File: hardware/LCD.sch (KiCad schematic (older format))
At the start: 23 parts, among them IC1 TPS61169DCKR, IC2 TPD4E001DRLR, IC3 AR1021-I/SS, U3 DS90CF364AMTD

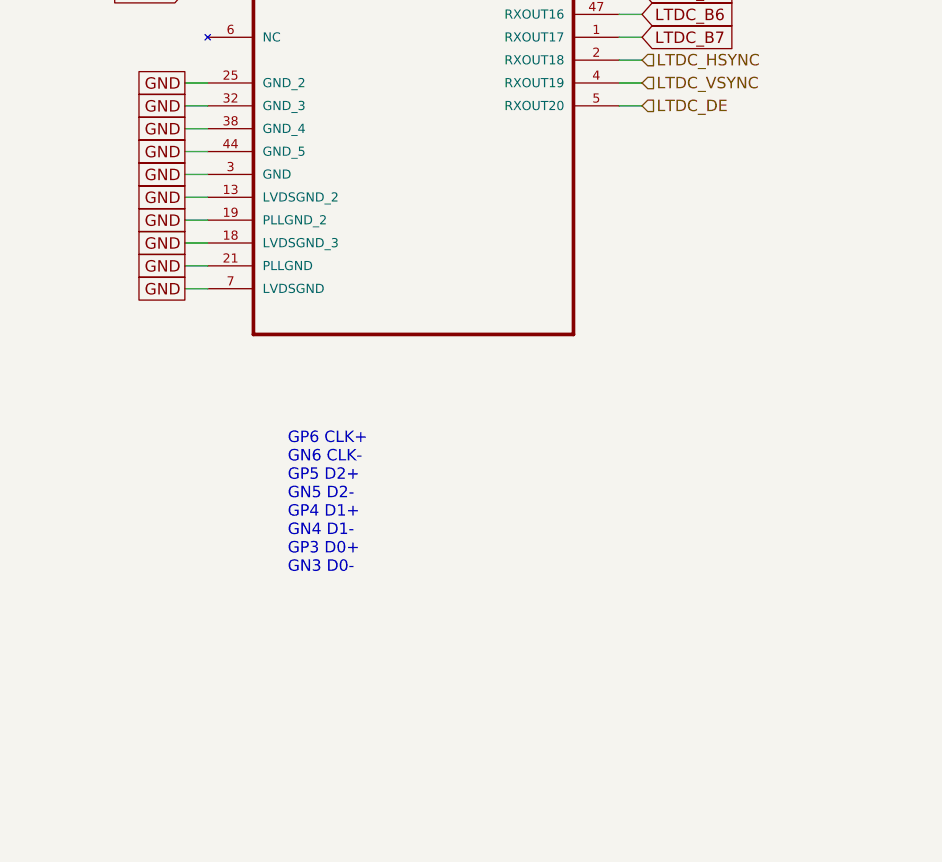
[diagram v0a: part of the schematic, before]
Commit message: Adding decoupling capacitors, termination resoistors for LVDS IN
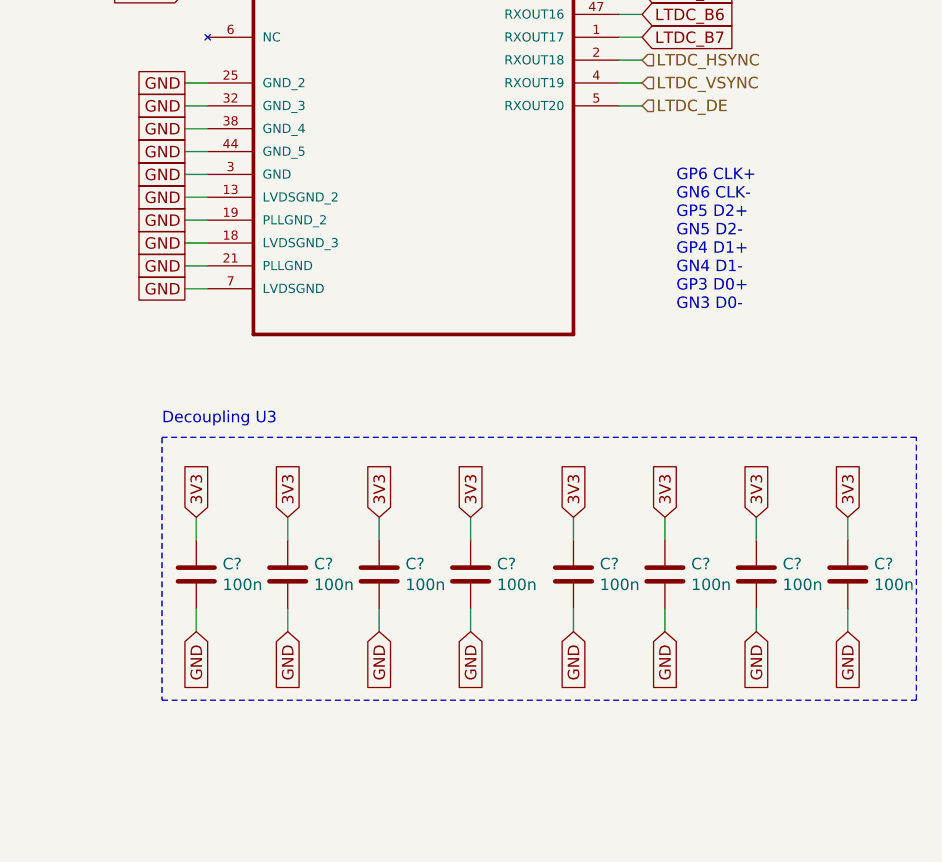
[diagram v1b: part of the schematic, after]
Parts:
- added C? (x8): 100n, symbol antena:C
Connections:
- net 3V3: now also C?.1, C?.1, C?.1, C?.1, C?.1, C?.1, C?.1, C?.1
- net GND: now also C?.2, C?.2, C?.2, C?.2, C?.2, C?.2, C?.2, C?.2
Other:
- note added: "Decoupling U3"
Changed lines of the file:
@@
 Wire Wire Line
 	9900 2350 10000 2350
-Text Notes 8450 5900 0    50   ~ 0
+Text Notes 10150 4750 0    50   ~ 0
 GP6 CLK+\nGN6 CLK-\nGP5 D2+\nGN5 D2-\nGP4 D1+\nGN4 D1-\nGP3 D0+\nGN3 D0-
 Text GLabel 8000 2350 0    50   Output ~ 0
@@
 Wire Wire Line
 	5500 7550 5650 7550
+Text GLabel 8000 3350 0    50   Input ~ 0
+~RESET
+Text GLabel 9700 5650 1    50   Input ~ 0
+3V3
+Text GLabel 9700 6150 3    50   Input ~ 0
+GND
+$Comp
+L antena:C C?
+U 1 1 5E384C70
+P 9700 5900
+AR Path="/5E22D431/5E384C70" Ref="C?"  Part="1"
+AR Path="/5E224865/5E384C70" Ref="C?"  Part="1"
+F 0 "C?" H 9815 5946 50  0000 L CNN
+F 1 "100n" H 9815 5855 50  0000 L CNN
+F 2 "" H 9738 5750 50  0001 C CNN
+F 3 "~" H 9700 5900 50  0001 C CNN
+	1    9700 5900
+	1    0    0    -1
+$EndComp
+Wire Wire Line
+	9700 5650 9700 5750
+Wire Wire Line
+	9700 6050 9700 6150
+Text GLabel 10100 5650 1    50   Input ~ 0
+3V3
+Text GLabel 10100 6150 3    50   Input ~ 0
+GND
+$Comp
+L antena:C C?
+U 1 1 5E384C7B
+P 10100 5900
+AR Path="/5E22D431/5E384C7B" Ref="C?"  Part="1"
+AR Path="/5E224865/5E384C7B" Ref="C?"  Part="1"
+F 0 "C?" H 10215 5946 50  0000 L CNN
+F 1 "100n" H 10215 5855 50  0000 L CNN
+F 2 "" H 10138 5750 50  0001 C CNN
+F 3 "~" H 10100 5900 50  0001 C CNN
+	1    10100 5900
+	1    0    0    -1
+$EndComp
+Wire Wire Line
+	10100 5650 10100 5750
+Wire Wire Line
+	10100 6050 10100 6150
+Text GLabel 10500 5650 1    50   Input ~ 0
+3V3
+Text GLabel 10500 6150 3    50   Input ~ 0
+GND
+$Comp
+L antena:C C?
+U 1 1 5E384C86
+P 10500 5900
+AR Path="/5E22D431/5E384C86" Ref="C?"  Part="1"
+AR Path="/5E224865/5E384C86" Ref="C?"  Part="1"
+F 0 "C?" H 10615 5946 50  0000 L CNN
+F 1 "100n" H 10615 5855 50  0000 L CNN
+F 2 "" H 10538 5750 50  0001 C CNN
+F 3 "~" H 10500 5900 50  0001 C CNN
+	1    10500 5900
+	1    0    0    -1
+$EndComp
+Wire Wire Line
+	10500 5650 10500 5750
+Wire Wire Line
+	10500 6050 10500 6150
+Text GLabel 10900 5650 1    50   Input ~ 0
+3V3
+Text GLabel 10900 6150 3    50   Input ~ 0
+GND
+$Comp
+L antena:C C?
+U 1 1 5E384C91
+P 10900 5900
+AR Path="/5E22D431/5E384C91" Ref="C?"  Part="1"
+AR Path="/5E224865/5E384C91" Ref="C?"  Part="1"
+F 0 "C?" H 11015 5946 50  0000 L CNN
+F 1 "100n" H 11015 5855 50  0000 L CNN
+F 2 "" H 10938 5750 50  0001 C CNN
+F 3 "~" H 10900 5900 50  0001 C CNN
+	1    10900 5900
+	1    0    0    -1
+$EndComp
+Wire Wire Line
+	10900 5650 10900 5750
+Wire Wire Line
+	10900 6050 10900 6150
+Text GLabel 8050 5650 1    50   Input ~ 0
+3V3
+Text GLabel 8050 6150 3    50   Input ~ 0
+GND
+$Comp
+L antena:C C?
+U 1 1 5E384C9C
+P 8050 5900
+AR Path="/5E22D431/5E384C9C" Ref="C?"  Part="1"
+AR Path="/5E224865/5E384C9C" Ref="C?"  Part="1"
+F 0 "C?" H 8165 5946 50  0000 L CNN
+F 1 "100n" H 8165 5855 50  0000 L CNN
+F 2 "" H 8088 5750 50  0001 C CNN
+F 3 "~" H 8050 5900 50  0001 C CNN
+	1    8050 5900
+	1    0    0    -1
+$EndComp
+Wire Wire Line
+	8050 5650 8050 5750
+Wire Wire Line
+	8050 6050 8050 6150
+Text GLabel 8450 5650 1    50   Input ~ 0
+3V3
+Text GLabel 8450 6150 3    50   Input ~ 0
+GND
+$Comp
+L antena:C C?
+U 1 1 5E384CA7
+P 8450 5900
+AR Path="/5E22D431/5E384CA7" Ref="C?"  Part="1"
+AR Path="/5E224865/5E384CA7" Ref="C?"  Part="1"
+F 0 "C?" H 8565 5946 50  0000 L CNN
+F 1 "100n" H 8565 5855 50  0000 L CNN
+F 2 "" H 8488 5750 50  0001 C CNN
+F 3 "~" H 8450 5900 50  0001 C CNN
+	1    8450 5900
+	1    0    0    -1
+$EndComp
+Wire Wire Line
+	8450 5650 8450 5750
+Wire Wire Line
+	8450 6050 8450 6150
+Text GLabel 8850 5650 1    50   Input ~ 0
+3V3
+Text GLabel 8850 6150 3    50   Input ~ 0
+GND
+$Comp
+L antena:C C?
+U 1 1 5E384CB2
+P 8850 5900
+AR Path="/5E22D431/5E384CB2" Ref="C?"  Part="1"
+AR Path="/5E224865/5E384CB2" Ref="C?"  Part="1"
+F 0 "C?" H 8965 5946 50  0000 L CNN
+F 1 "100n" H 8965 5855 50  0000 L CNN
+F 2 "" H 8888 5750 50  0001 C CNN
+F 3 "~" H 8850 5900 50  0001 C CNN
+	1    8850 5900
+	1    0    0    -1
+$EndComp
+Wire Wire Line
+	8850 5650 8850 5750
+Wire Wire Line
+	8850 6050 8850 6150
+Text GLabel 9250 5650 1    50   Input ~ 0
+3V3
+Text GLabel 9250 6150 3    50   Input ~ 0
+GND
+$Comp
+L antena:C C?
+U 1 1 5E384CBD
+P 9250 5900
+AR Path="/5E22D431/5E384CBD" Ref="C?"  Part="1"
+AR Path="/5E224865/5E384CBD" Ref="C?"  Part="1"
+F 0 "C?" H 9365 5946 50  0000 L CNN
+F 1 "100n" H 9365 5855 50  0000 L CNN
+F 2 "" H 9288 5750 50  0001 C CNN
+F 3 "~" H 9250 5900 50  0001 C CNN
+	1    9250 5900
+	1    0    0    -1
+$EndComp
+Wire Wire Line
+	9250 5650 9250 5750
+Wire Wire Line
+	9250 6050 9250 6150
+Wire Notes Line
+	11200 6450 11200 5300
+Wire Notes Line
+	11200 5300 7900 5300
+Wire Notes Line
+	7900 5300 7900 6450
+Wire Notes Line
+	7900 6450 11200 6450
 Wire Bus Line
 	6175 2700 6175 3200
@@
 Wire Bus Line
 	6175 1900 6175 2400
-Text GLabel 8000 3350 0    50   Input ~ 0
-~RESET
+Text Notes 7900 5250 0    50   ~ 0
+Decoupling U3
 $EndSCHEMATC

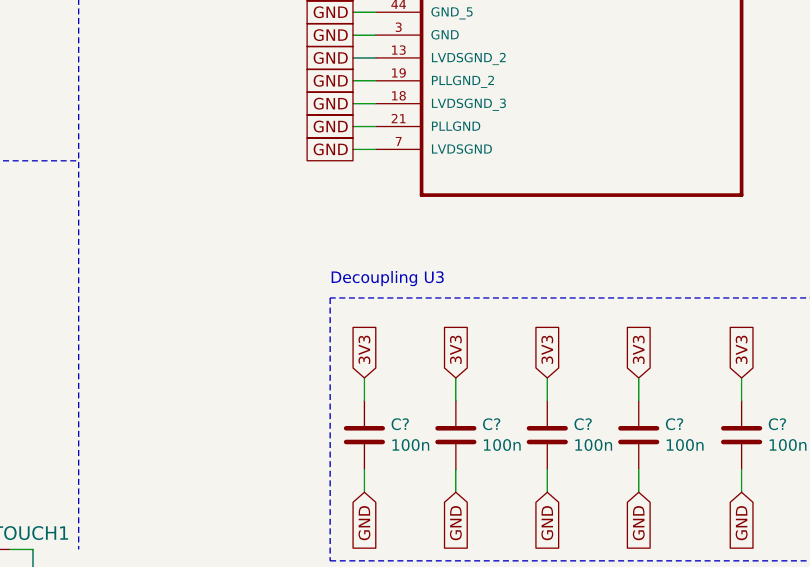
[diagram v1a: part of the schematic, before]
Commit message: Adding selection resistors
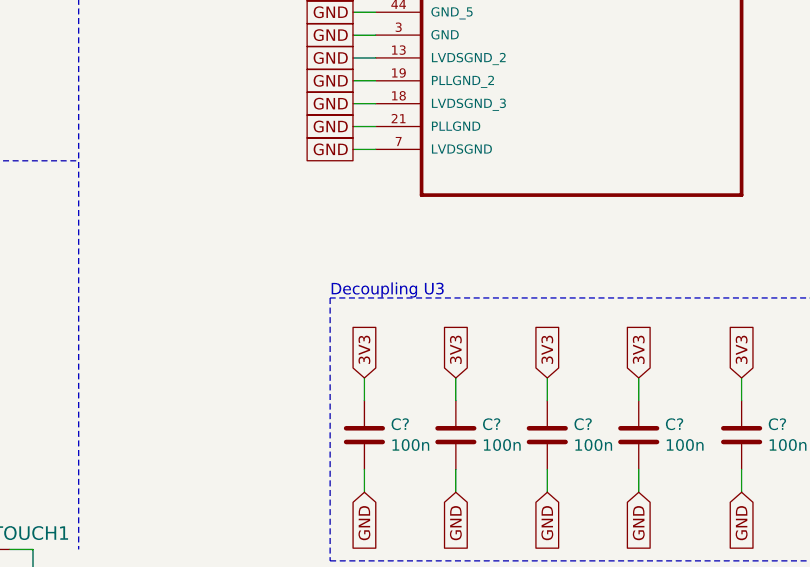
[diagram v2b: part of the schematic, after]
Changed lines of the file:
@@
 Wire Notes Line
 	7900 6450 11200 6450
+Text Notes 7900 5300 0    50   ~ 0
+Decoupling U3
 Wire Bus Line
 	6175 2700 6175 3200
@@
 Wire Bus Line
 	6175 1900 6175 2400
-Text Notes 7900 5250 0    50   ~ 0
-Decoupling U3
 $EndSCHEMATC

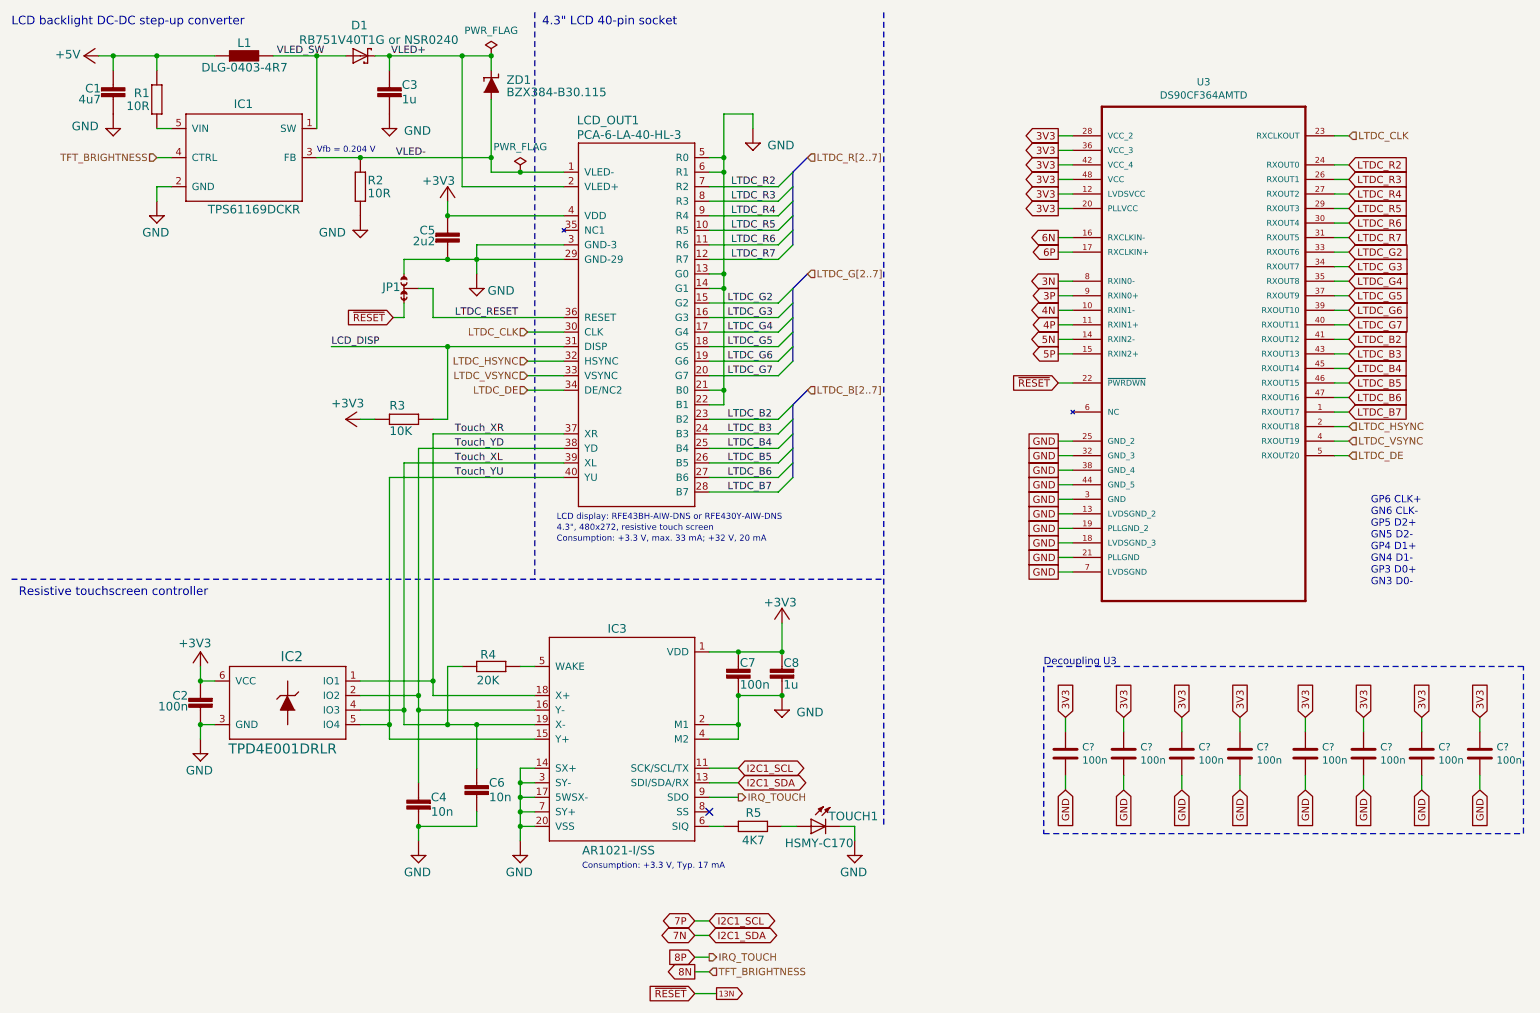
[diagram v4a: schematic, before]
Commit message: Adding ULX3S connections
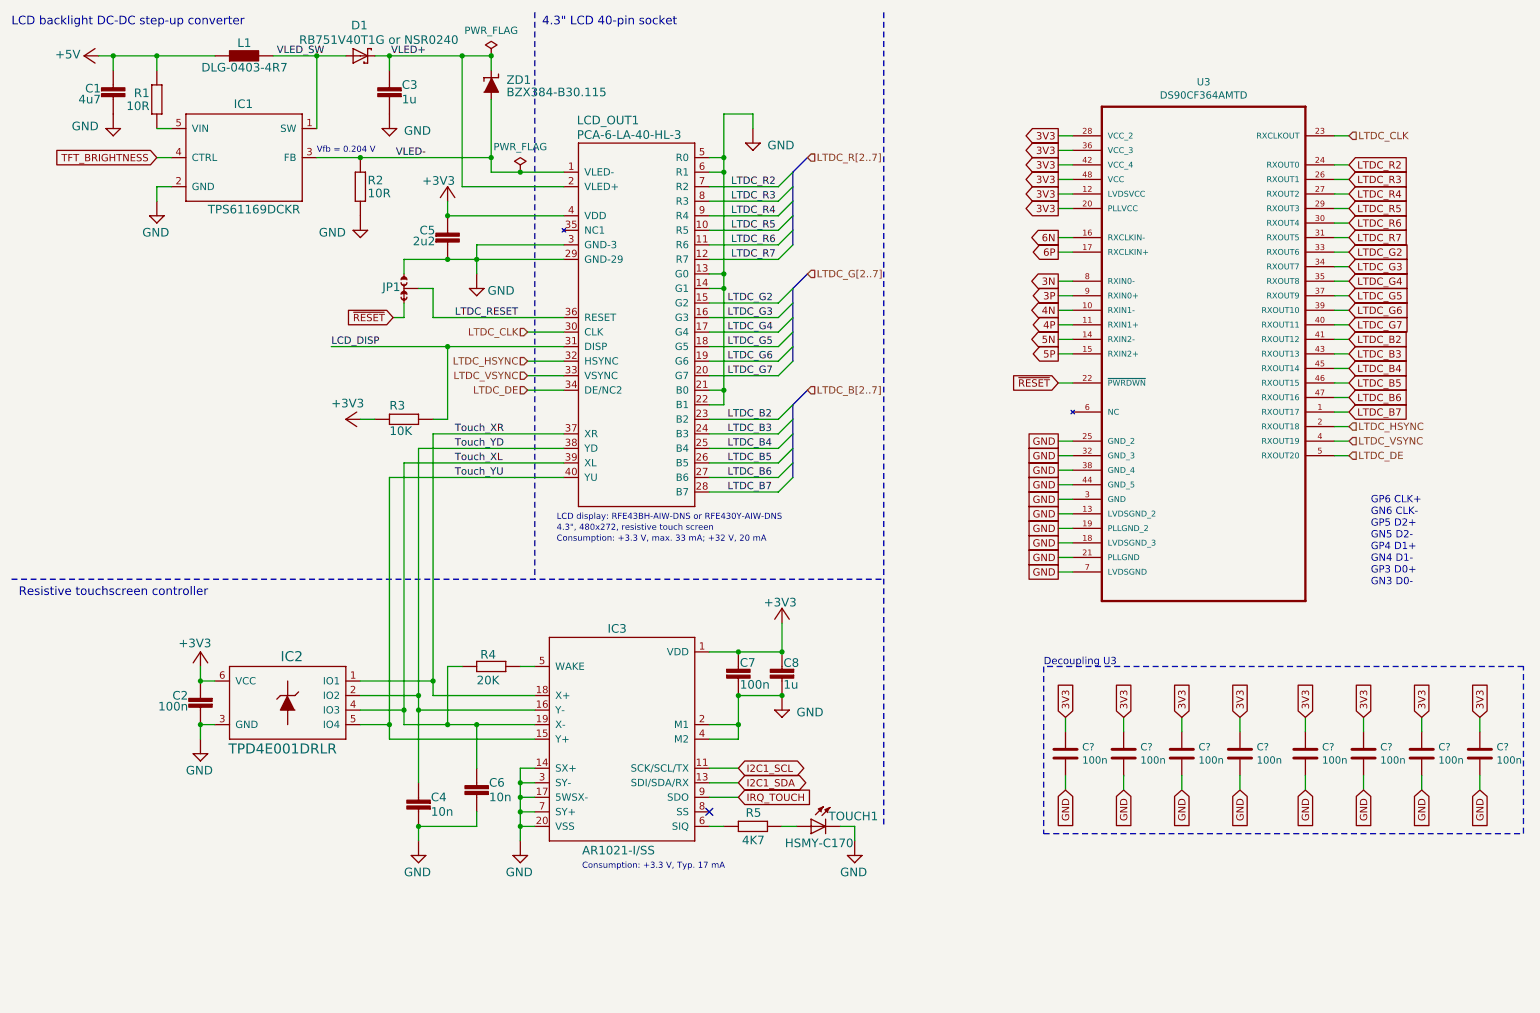
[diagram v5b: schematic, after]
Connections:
- net 13N renamed ~RESET
- net 7N renamed I2C1_SDA
- net 7P renamed I2C1_SCL
- net 8N renamed TFT_BRIGHTNESS
- net 8P renamed IRQ_TOUCH
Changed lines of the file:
@@
 Text HLabel 4350 3400 0    50   Input ~ 0
 LTDC_DE
-Text HLabel 1800 1800 0    50   Input ~ 0
-TFT_BRIGHTNESS
 $Comp
 L power:PWR_FLAG #FLG0101
@@
 Wire Wire Line
 	4300 1900 4600 1900
-Text HLabel 5800 6200 2    50   Output ~ 0
-IRQ_TOUCH
 Text Label 3850 3700 0    50   ~ 0
 Touch_XR
@@
 Wire Wire Line
 	8000 2050 8100 2050
-Text GLabel 5500 7050 0    50   BiDi ~ 0
-7P
-Text GLabel 5500 7150 0    50   BiDi ~ 0
-7N
-Text GLabel 5600 7050 2    50   BiDi ~ 0
-I2C1_SCL
-Text GLabel 5600 7150 2    50   BiDi ~ 0
-I2C1_SDA
-Wire Wire Line
-	5500 7050 5600 7050
-Wire Wire Line
-	5500 7150 5600 7150
-Text HLabel 5600 7300 2    50   Output ~ 0
-IRQ_TOUCH
-Text GLabel 5500 7300 0    50   Input ~ 0
-8P
-Wire Wire Line
-	5500 7300 5600 7300
-Text GLabel 5500 7400 0    50   Output ~ 0
-8N
-Text HLabel 5600 7400 2    50   Input ~ 0
-TFT_BRIGHTNESS
-Wire Wire Line
-	5500 7400 5600 7400
-Text GLabel 5500 7550 0    50   Input ~ 0
-~RESET
 Wire Wire Line
 	8000 3350 8100 3350
-Text GLabel 5650 7550 2    39   Output ~ 0
-13N
-Wire Wire Line
-	5500 7550 5650 7550
 Text GLabel 8000 3350 0    50   Input ~ 0
 ~RESET
@@
 Text Notes 7900 5300 0    50   ~ 0
 Decoupling U3
+Text GLabel 5800 6200 2    50   Input ~ 0
+IRQ_TOUCH
+Text GLabel 1800 1800 0    50   Input ~ 0
+TFT_BRIGHTNESS
 Wire Bus Line
 	6175 2700 6175 3200
